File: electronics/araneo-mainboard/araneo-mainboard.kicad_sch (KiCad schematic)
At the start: 88 parts, among them IC1 TPS54302DDCR, IC2 BMI270, IC3 MMC5983MA, J2 OLED, J3 GPIO, SW2 SW, SW3 SW, U4 POWER, U5 PAM8403D, U6 3V3

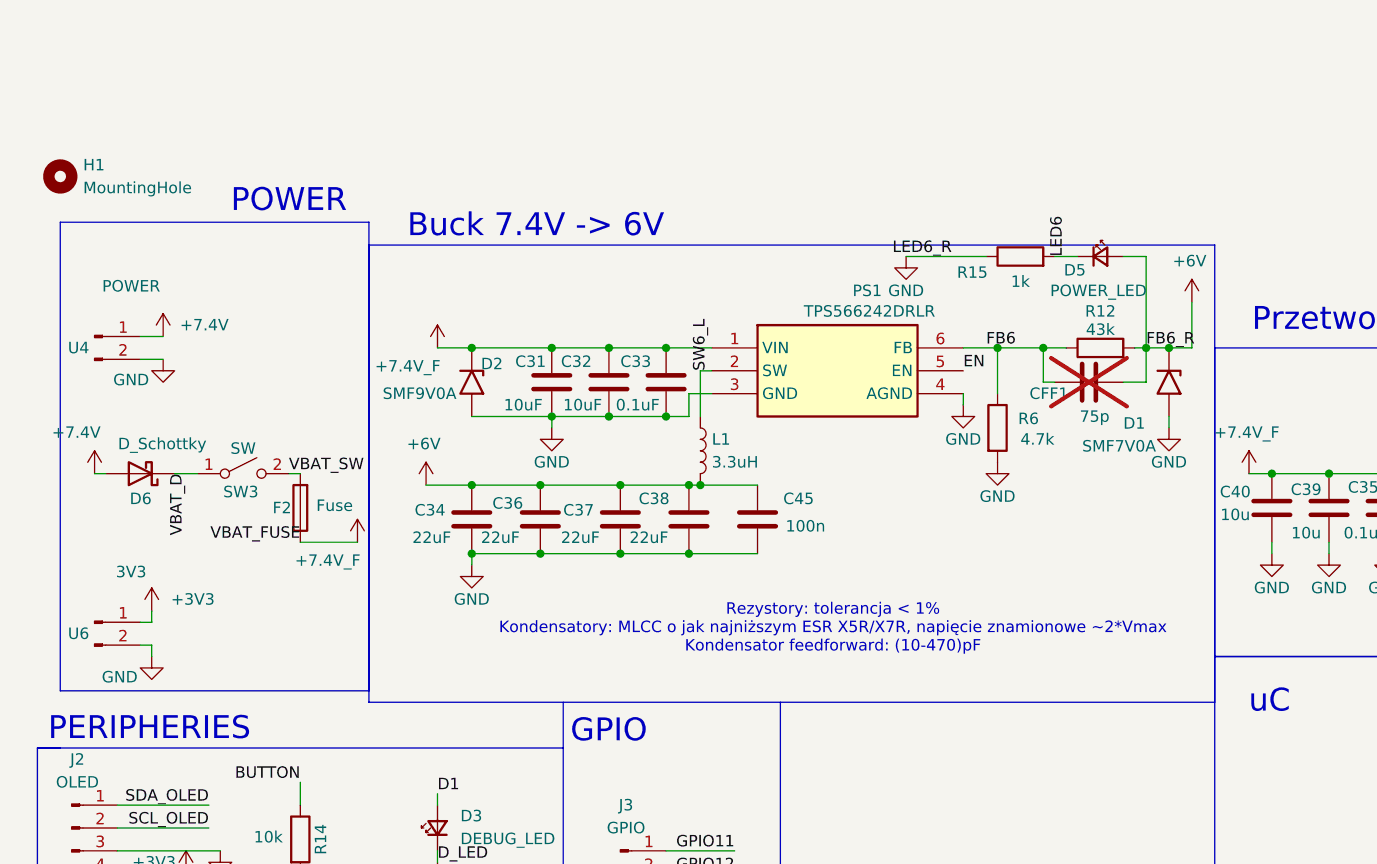
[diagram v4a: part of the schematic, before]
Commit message: electronics: change 22u footprint
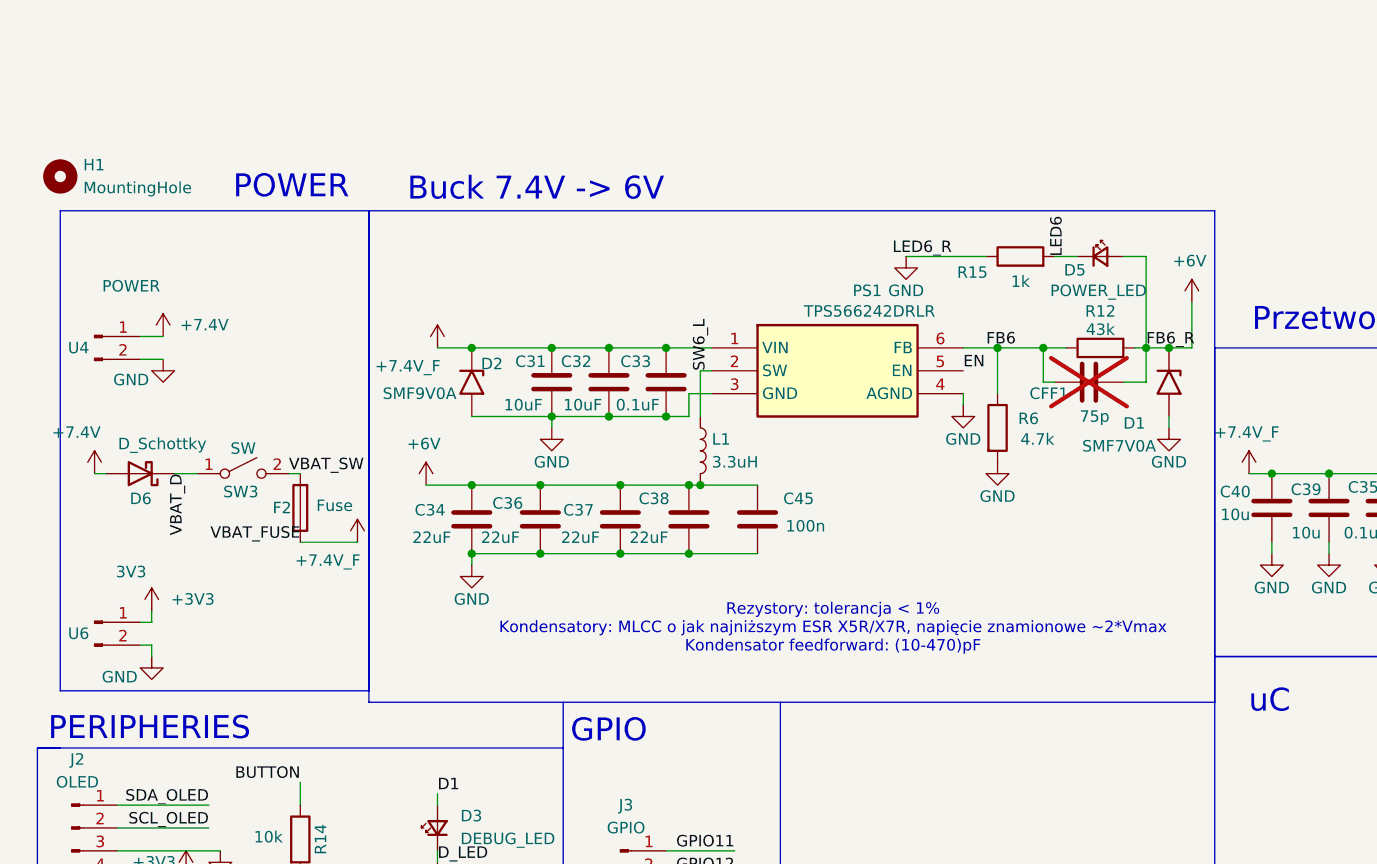
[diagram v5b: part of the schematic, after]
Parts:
- C29, C30, C36, C37, C38: footprint Capacitor_SMD:C_0603_1608Metric_Pad1.08x0.95mm_HandSolder -> Capacitor_SMD:C_0805_2012Metric_Pad1.18x1.45mm_HandSolder
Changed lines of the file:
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@@
 	)
 	(rectangle
-		(start 49.53 24.13)
+		(start 49.53 20.32)
 		(end 143.51 74.93)
 		(stroke
@@
 	)
 	(rectangle
-		(start 15.24 21.59)
+		(start 15.24 20.32)
 		(end 49.53 73.66)
 		(stroke
@@
 	(text "POWER"
 		(exclude_from_sim no)
-		(at 40.64 19.304 0)
+		(at 40.894 17.78 0)
 		(effects
 			(font
@@
 	(text "Buck 7.4V -> 6V"
 		(exclude_from_sim no)
-		(at 68.072 22.098 0)
+		(at 68.072 18.034 0)
 		(effects
 			(font
@@
 			)
 		)
-		(property "Footprint" "Capacitor_SMD:C_0603_1608Metric_Pad1.08x0.95mm_HandSolder"
+		(property "Footprint" "Capacitor_SMD:C_0805_2012Metric_Pad1.18x1.45mm_HandSolder"
 			(at 219.4052 64.77 0)
 			(hide yes)
@@
 			)
 		)
-		(property "Footprint" "Capacitor_SMD:C_0603_1608Metric_Pad1.08x0.95mm_HandSolder"
+		(property "Footprint" "Capacitor_SMD:C_0805_2012Metric_Pad1.18x1.45mm_HandSolder"
 			(at 69.5452 58.42 0)
 			(hide yes)
@@
 			)
 		)
-		(property "Footprint" "Capacitor_SMD:C_0603_1608Metric_Pad1.08x0.95mm_HandSolder"
+		(property "Footprint" "Capacitor_SMD:C_0805_2012Metric_Pad1.18x1.45mm_HandSolder"
 			(at 225.7552 64.77 0)
 			(hide yes)
@@
 			)
 		)
-		(property "Footprint" "Capacitor_SMD:C_0603_1608Metric_Pad1.08x0.95mm_HandSolder"
+		(property "Footprint" "Capacitor_SMD:C_0805_2012Metric_Pad1.18x1.45mm_HandSolder"
 			(at 86.0552 58.42 0)
 			(hide yes)
@@
 			)
 		)
-		(property "Footprint" "Capacitor_SMD:C_0603_1608Metric_Pad1.08x0.95mm_HandSolder"
+		(property "Footprint" "Capacitor_SMD:C_0805_2012Metric_Pad1.18x1.45mm_HandSolder"
 			(at 78.4352 58.42 0)
 			(hide yes)

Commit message: electronics: move uC to have USB inlined with border
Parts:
- removed C19: 0.1uF, Capacitor_SMD:C_0603_1608Metric_Pad1.08x0.95mm_HandSolder, symbol Device:C
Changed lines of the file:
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@@
 	)
 	(junction
-		(at 22.86 93.98)
-		(diameter 0)
-		(color 0 0 0 0)
-	)
-	(junction
 		(at 351.79 80.01)
 		(diameter 0)
@@
 	(wire
 		(pts
-			(xy 22.86 105.41) (xy 22.86 101.6)
-		)
-		(stroke
-			(width 0)
-			(type default)
-		)
-	)
-	(wire
-		(pts
 			(xy 85.09 40.64) (xy 85.09 43.18)
 		)
@@
 	(wire
 		(pts
-			(xy 22.86 93.98) (xy 29.21 93.98)
+			(xy 21.59 93.98) (xy 29.21 93.98)
 		)
 		(stroke
@@
 	(wire
 		(pts
-			(xy 21.59 93.98) (xy 22.86 93.98)
-		)
-		(stroke
-			(width 0)
-			(type default)
-		)
-	)
-	(wire
-		(pts
 			(xy 330.2 173.99) (xy 330.2 176.53)
 		)
@@
 	)
 	(symbol
-		(lib_id "power:GND")
-		(at 22.86 105.41 0)
-		(unit 1)
-		(body_style 1)
-		(exclude_from_sim no)
-		(in_bom yes)
-		(on_board yes)
-		(in_pos_files yes)
-		(dnp no)
-		(fields_autoplaced yes)
-		(property "Reference" "#PWR039"
-			(at 22.86 111.76 0)
-			(hide yes)
-			(show_name no)
-			(do_not_autoplace no)
-			(effects
-				(font
-					(size 1.27 1.27)
-				)
-			)
-		)
-		(property "Value" "GND"
-			(at 22.86 110.49 0)
-			(show_name no)
-			(do_not_autoplace no)
-			(effects
-				(font
-					(size 1.27 1.27)
-				)
-			)
-		)
-		(property "Footprint" ""
-			(at 22.86 105.41 0)
-			(hide yes)
-			(show_name no)
-			(do_not_autoplace no)
-			(effects
-				(font
-					(size 1.27 1.27)
-				)
-			)
-		)
-		(property "Datasheet" ""
-			(at 22.86 105.41 0)
-			(hide yes)
-			(show_name no)
-			(do_not_autoplace no)
-			(effects
-				(font
-					(size 1.27 1.27)
-				)
-			)
-		)
-		(property "Description" "Power symbol creates a global label with name \"GND\" , ground"
-			(at 22.86 105.41 0)
-			(hide yes)
-			(show_name no)
-			(do_not_autoplace no)
-			(effects
-				(font
-					(size 1.27 1.27)
-				)
-			)
-		)
-		(pin "1"
-		)
-		(instances
-			(project "araneo-mainboard"
-				(path "/0ff7269e-d15c-4d73-8399-8898e55a410d"
-					(reference "#PWR039")
-					(unit 1)
-				)
-			)
-		)
-	)
-	(symbol
 		(lib_id "Mechanical:MountingHole")
 		(at 15.24 16.51 0)
@@
 					(unit 1)
 				)
-			)
-		)
-	)
-	(symbol
-		(lib_id "Device:C")
-		(at 22.86 97.79 0)
-		(unit 1)
-		(body_style 1)
-		(exclude_from_sim no)
-		(in_bom yes)
-		(on_board yes)
-		(in_pos_files yes)
-		(dnp no)
-		(property "Reference" "C19"
-			(at 26.162 96.774 0)
-			(show_name no)
-			(do_not_autoplace no)
-			(effects
-				(font
-					(size 1.27 1.27)
-				)
-				(justify left)
-			)
-		)
-		(property "Value" "0.1uF"
-			(at 26.416 99.06 0)
-			(show_name no)
-			(do_not_autoplace no)
-			(effects
-				(font
-					(size 1.27 1.27)
-				)
-				(justify left)
-			)
-		)
-		(property "Footprint" "Capacitor_SMD:C_0603_1608Metric_Pad1.08x0.95mm_HandSolder"
-			(at 23.8252 101.6 0)
-			(hide yes)
-			(show_name no)
-			(do_not_autoplace no)
-			(effects
-				(font
-					(size 1.27 1.27)
-				)
-			)
-		)
-		(property "Datasheet" ""
-			(at 22.86 97.79 0)
-			(hide yes)
-			(show_name no)
-			(do_not_autoplace no)
-			(effects
-				(font
-					(size 1.27 1.27)
-				)
-			)
-		)
-		(property "Description" "Unpolarized capacitor"
-			(at 22.86 97.79 0)
-			(hide yes)
-			(show_name no)
-			(do_not_autoplace no)
-			(effects
-				(font
-					(size 1.27 1.27)
-				)
-			)
-		)
-		(pin "1"
-		)
-		(pin "2"
-		)
-		(instances
-			(project "araneo-mainboard"
-				(path "/0ff7269e-d15c-4d73-8399-8898e55a410d"
-					(reference "C19")
-					(unit 1)
-				)

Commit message: araneo mainboard v2 schematic preparation
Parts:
- removed A1: RaspberryPi_Pico_2W, Pico:RaspberryPi_Pico_Common_THT_MountingHoles, symbol Pico:RaspberryPi_Pico_W
- removed C1, C20, C35, C42, C5, C9: 0.1u, Capacitor_SMD:C_0603_1608Metric_Pad1.08x0.95mm_HandSolder, symbol Device:C
- removed C10, C33: 0.1uF, Capacitor_SMD:C_0603_1608Metric_Pad1.08x0.95mm_HandSolder, symbol Device:C
- removed C11, C12: 220pF, Capacitor_SMD:C_0603_1608Metric_Pad1.08x0.95mm_HandSolder, symbol Device:C
- removed C13, C14: 0.47uF, Capacitor_SMD:C_0603_1608Metric_Pad1.08x0.95mm_HandSolder, symbol Device:C
- removed C15, C16, C18: 1uF, Capacitor_SMD:C_0603_1608Metric_Pad1.08x0.95mm_HandSolder, symbol Device:C
- removed C17: 470uF, Capacitor_THT:CP_Radial_D10.0mm_P5.00mm, symbol Device:C
- removed C2, C39, C40: 10u, Capacitor_SMD:C_0603_1608Metric_Pad1.08x0.95mm_HandSolder, symbol Device:C
- removed C29, C30: 22u, Capacitor_SMD:C_0805_2012Metric_Pad1.18x1.45mm_HandSolder, symbol Device:C
- removed C3, C4, C43: 1u, Capacitor_SMD:C_0603_1608Metric_Pad1.08x0.95mm_HandSolder, symbol Device:C
- removed C31, C32: 10uF, Capacitor_SMD:C_0603_1608Metric_Pad1.08x0.95mm_HandSolder, symbol Device:C
- removed C34: 22uF, Capacitor_SMD:C_0603_1608Metric_Pad1.08x0.95mm_HandSolder, symbol Device:C
- removed C36, C37, C38: 22uF, Capacitor_SMD:C_0805_2012Metric_Pad1.18x1.45mm_HandSolder, symbol Device:C
- removed C41, CFF1: 75p, Capacitor_SMD:C_0603_1608Metric_Pad1.08x0.95mm_HandSolder, symbol Device:C
- removed C44, C45: 100n, Capacitor_SMD:C_0603_1608Metric_Pad1.08x0.95mm_HandSolder, symbol Device:C
- removed D1: SMF7V0A, Diode_SMD:D_SOD-123, symbol Diode:SMF7V0A
- removed D2: SMF9V0A, Diode_SMD:D_SMF, symbol Diode:SMF9V0A
- removed D3: DEBUG_LED, PCM_SparkFun-LED:LED_0603_1608Metric, symbol PCM_SparkFun-LED:LED
- removed D5: POWER_LED, PCM_SparkFun-LED:LED_0603_1608Metric, symbol PCM_SparkFun-LED:LED
- removed D6: D_Schottky, Diode_THT:D_DO-41_SOD81_P10.16mm_Horizontal, symbol Device:D_Schottky
- removed F2: Fuse, custom_footprints:3568, symbol Device:Fuse
- removed FB3, FB4: FerriteBead, Resistor_SMD:R_0603_1608Metric_Pad0.98x0.95mm_HandSolder, symbol Device:FerriteBead
- removed H1, H2, H3, H4: MountingHole, MountingHole:MountingHole_3.2mm_M3, symbol Mechanical:MountingHole
- removed IC1: TPS54302DDCR, custom_footprints:SOT95P280X110-6N, symbol Symbols:TPS54302DDCR
- removed IC2: BMI270, custom_footprints:BMI270, symbol Symbols:BMI270
- removed IC3: MMC5983MA, custom_footprints:MMC5983MA, symbol Symbols:MMC5983MA
- removed J2: OLED, Connector_JST:JST_XH_B4B-XH-A_1x04_P2.50mm_Vertical, symbol Connector:Conn_01x04_Pin
- removed J3: GPIO, Connector_PinHeader_2.54mm:PinHeader_1x05_P2.54mm_Vertical, symbol Connector:Conn_01x05_Pin
- removed L1: 3.3uH, custom_footprints:INDPM112100X400N, symbol Device:L
- removed L2: 10u, custom_footprints:PA4302103NLT, symbol Device:L
- removed LS1: Speaker, PCM_SparkFun-Connector:ScrewTerminal_1x02_P3.5mm_Blue, symbol Device:Speaker
- removed PS1: TPS566242DRLR, custom_footprints:SOT50P160X60-6N, symbol Symbols:TPS566242DRLR
- removed R1, R10, R18, R19, R2, R3, R4, R6, R9: 4.7k, Resistor_SMD:R_0603_1608Metric_Pad0.98x0.95mm_HandSolder, symbol Device:R
- removed R11, R14: 10k, Resistor_SMD:R_0603_1608Metric_Pad0.98x0.95mm_HandSolder, symbol Device:R
- removed R12: 43k, Resistor_SMD:R_0603_1608Metric_Pad0.98x0.95mm_HandSolder, symbol Device:R
- removed R13, R15: 1k, Resistor_SMD:R_0603_1608Metric_Pad0.98x0.95mm_HandSolder, symbol Device:R
- removed R16: 100k, Resistor_SMD:R_0603_1608Metric_Pad0.98x0.95mm_HandSolder, symbol Device:R
- removed R17: 13.3k, Resistor_SMD:R_0603_1608Metric_Pad0.98x0.95mm_HandSolder, symbol Device:R
- removed R20, R21: 0, Resistor_SMD:R_0603_1608Metric_Pad0.98x0.95mm_HandSolder, symbol Device:R
- removed S1: Servo1, Connector_PinHeader_2.54mm:PinHeader_1x03_P2.54mm_Vertical, symbol Connector:Conn_01x03_Pin
- removed S2: Servo2, Connector_PinHeader_2.54mm:PinHeader_1x03_P2.54mm_Vertical, symbol Connector:Conn_01x03_Pin
- removed S3: Servo3, Connector_PinHeader_2.54mm:PinHeader_1x03_P2.54mm_Vertical, symbol Connector:Conn_01x03_Pin
- removed S4: Servo4, Connector_PinHeader_2.54mm:PinHeader_1x03_P2.54mm_Vertical, symbol Connector:Conn_01x03_Pin
- removed S5: Servo5, Connector_PinHeader_2.54mm:PinHeader_1x03_P2.54mm_Vertical, symbol Connector:Conn_01x03_Pin
- removed S6: Servo6, Connector_PinHeader_2.54mm:PinHeader_1x03_P2.54mm_Vertical, symbol Connector:Conn_01x03_Pin
- removed S7: Servo7, Connector_PinHeader_2.54mm:PinHeader_1x03_P2.54mm_Vertical, symbol Connector:Conn_01x03_Pin
- removed S8: Servo8, Connector_PinHeader_2.54mm:PinHeader_1x03_P2.54mm_Vertical, symbol Connector:Conn_01x03_Pin
- removed SW2: SW, PCM_SparkFun-Connector:ScrewTerminal_1x02_P3.5mm_Blue, symbol Switch:SW_SPST
- removed SW3: SW, PCM_SparkFun-Connector:ScrewTerminal_1x02_P5.0mm, symbol Switch:SW_SPST
- removed U4: POWER, Connector_AMASS:AMASS_XT30U-M_1x02_P5.0mm_Vertical, symbol Connector:Conn_01x02_Pin
- removed U5: PAM8403D, Package_SO:SOIC-16_3.9x9.9mm_P1.27mm, symbol Amplifier_Audio:PAM8403D
- removed U6: 3V3, Connector_PinHeader_2.54mm:PinHeader_1x02_P2.54mm_Vertical, symbol Connector:Conn_01x02_Pin
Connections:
- no-connect marks 20 -> 0
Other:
- added sheet IMU (imu.kicad_sch)
- added sheet MCU (mcu.kicad_sch)
- added sheet Magnetometer (magnetometer.kicad_sch)
- added sheet Power (power.kicad_sch)
- added sheet Power 6V (servo_power.kicad_sch)
- added sheet Servos (servos.kicad_sch)
- added sheet Speaker (speaker.kicad_sch)
- note removed: "Buck 7.4V -> 6V"
- note removed: "Dzielnik dobrany jak tu:"
- note removed: "GPIO"
- note removed: "IMU"
- note removed: "MAGNETOMETER"
- note removed: "PERIPHERIES"
- note removed: "POWER"
- note removed: "Przetwornica 7.4V -> 5V"
- note removed: "Rezystory: tolerancja < 1% Kondensatory: MLCC o jak najniższym ESR X5R/X7R, napięcie znamionowe ~2*Vmax Kondensator feedforward: (10-470)pF"
- note removed: "Vin, GND - jak największe Kondensatory jak najbliżej Ścieżka SW - jak najkrótsza i dość szeroka Ścieżka FB - jak najkrótsza i osobna ścieżka GND i Vout Dużo GND do odprowadzania ciepła Dioda TVS dla szpilek napięcia przy podłączaniu (> 15V)"
- note removed: "Wartości rezystorów z datasheet Kondensatory MLCC z niskim ESR"
- note removed: "uC"
- company: KoNaR -> (none)
- title: Araneo Electronics -> (none)

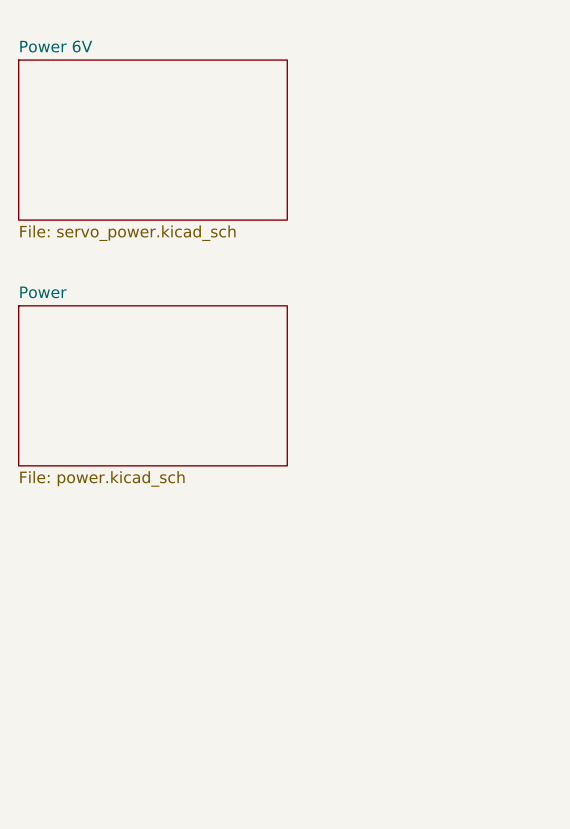
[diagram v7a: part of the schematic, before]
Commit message: add components schematics
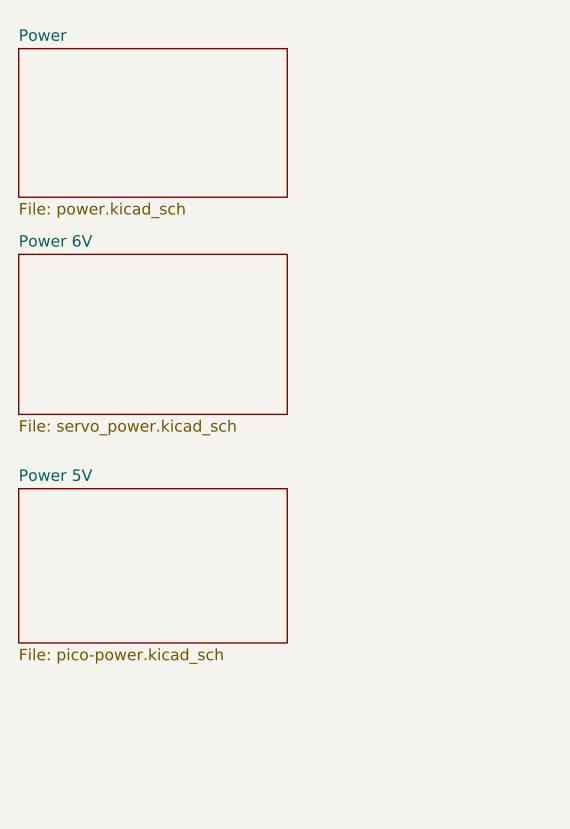
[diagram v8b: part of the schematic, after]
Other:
- added sheet Power 5V (pico-power.kicad_sch)
- company: (none) -> KoNaR
- title: (none) -> Araneo Main Board
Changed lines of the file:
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@@
 	(generator_version "10.0")
 	(paper "A4")
+	(title_block
+		(title "Araneo Main Board")
+		(rev "1")
+		(company "KoNaR")
+		(comment 1 "Michal Sadecki")
+	)
 	(sheet
 		(at 219.71 88.9)
@@
 	)
 	(sheet
-		(at 46.99 67.945)
-		(size 29.845 17.78)
-		(exclude_from_sim no)
-		(in_bom yes)
-		(on_board yes)
-		(dnp no)
-		(fields_autoplaced yes)
-		(stroke
-			(width 0.1524)
-			(type solid)
-		)
-		(fill
-			(color 0 0 0 0)
-		)
-		(property "Sheetname" "Power"
-			(at 46.99 67.2334 0)
-			(show_name no)
-			(do_not_autoplace no)
-			(effects
-				(font
-					(size 1.27 1.27)
-				)
-				(justify left bottom)
-			)
-		)
-		(property "Sheetfile" "power.kicad_sch"
-			(at 46.99 86.3096 0)
-			(show_name no)
-			(do_not_autoplace no)
-			(effects
-				(font
-					(size 1.27 1.27)
-				)
-				(justify left top)
-			)
-		)
-		(instances
-			(project "araneo-mainboard"
-				(path "/f9fcb57c-0831-41d4-a374-fa7a29fb9e88"
-					(page "8")
-				)
-			)
-		)
-	)
-	(sheet
 		(at 219.71 40.005)
 		(size 26.035 15.875)
@@
 	)
 	(sheet
+		(at 46.99 39.37)
+		(size 29.845 16.51)
+		(exclude_from_sim no)
+		(in_bom yes)
+		(on_board yes)
+		(dnp no)
+		(fields_autoplaced yes)
+		(stroke
+			(width 0.1524)
+			(type solid)
+		)
+		(fill
+			(color 0 0 0 0)
+		)
+		(property "Sheetname" "Power"
+			(at 46.99 38.6584 0)
+			(show_name no)
+			(do_not_autoplace no)
+			(effects
+				(font
+					(size 1.27 1.27)
+				)
+				(justify left bottom)
+			)
+		)
+		(property "Sheetfile" "power.kicad_sch"
+			(at 46.99 56.4646 0)
+			(show_name no)
+			(do_not_autoplace no)
+			(effects
+				(font
+					(size 1.27 1.27)
+				)
+				(justify left top)
+			)
+		)
+		(instances
+			(project "araneo-mainboard"
+				(path "/f9fcb57c-0831-41d4-a374-fa7a29fb9e88"
+					(page "9")
+				)
+			)
+		)
+	)
+	(sheet
+		(at 46.99 88.265)
+		(size 29.845 17.145)
+		(exclude_from_sim no)
+		(in_bom yes)
+		(on_board yes)
+		(dnp no)
+		(fields_autoplaced yes)
+		(stroke
+			(width 0.1524)
+			(type solid)
+		)
+		(fill
+			(color 0 0 0 0)
+		)
+		(property "Sheetname" "Power 5V"
+			(at 46.99 87.5534 0)
+			(show_name no)
+			(do_not_autoplace no)
+			(effects
+				(font
+					(size 1.27 1.27)
+				)
+				(justify left bottom)
+			)
+		)
+		(property "Sheetfile" "pico-power.kicad_sch"
+			(at 46.99 105.9946 0)
+			(show_name no)
+			(do_not_autoplace no)
+			(effects
+				(font
+					(size 1.27 1.27)
+				)
+				(justify left top)
+			)
+		)
+		(instances
+			(project "araneo-mainboard"
+				(path "/f9fcb57c-0831-41d4-a374-fa7a29fb9e88"
+					(page "8")
+				)
+			)
+		)
+	)
+	(sheet
 		(at 219.71 64.77)
 		(size 26.035 15.24)
@@
 	)
 	(sheet
-		(at 46.99 40.64)
+		(at 46.99 62.23)
 		(size 29.845 17.78)
 		(exclude_from_sim no)
@@
 		)
 		(property "Sheetname" "Power 6V"
-			(at 46.99 39.9284 0)
+			(at 46.99 61.5184 0)
 			(show_name no)
 			(do_not_autoplace no)
@@
 		)
 		(property "Sheetfile" "servo_power.kicad_sch"
-			(at 46.99 59.0046 0)
-			(show_name no)
-			(do_not_autoplace no)
+			(at 46.99 80.5946 0)
+			(show_name no)
+			(do_not_autoplace no)
